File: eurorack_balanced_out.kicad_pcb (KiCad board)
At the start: 2 copper layers, 60 x 35 mm, 31 parts, among them J1 Conn_01x02, J2 Conn_01x02, J3 Conn_02x05_Odd_Even, J4 AudioJack3, J5 AudioJack3, U1 THAT1646W16, U2 THAT1646W16

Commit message: more cleanup
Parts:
- moved D2 1.00 mm to (164.5, 147.0)
- moved D4 1.00 mm to (169.5, 147.0)
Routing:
- net Vcc: track 24.3 -> 0.00 mm, vias 1 -> 0
- net Vee: track 26.3 -> 6.50 mm, vias 1 -> 0
- net Net-(C5-Pad1): track 15.2 -> 24.0 mm
- net Net-(R2-Pad1): track 7.60 -> 4.60 mm
- net Net-(R1-Pad1): track 7.60 -> 4.60 mm
- net Net-(C7-Pad1): track 23.9 -> 25.0 mm
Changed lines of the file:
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@@
     (thickness 1.6)
     (drawings 4)
-    (tracks 95)
+    (tracks 84)
     (zones 0)
     (modules 31)
@@
   (layers
     (0 F.Cu signal)
-    (31 B.Cu signal)
+    (31 B.Cu signal hide)
     (32 B.Adhes user)
     (33 F.Adhes user)
@@
   )
   (module Package_TO_SOT_SMD:SOT-23 (layer F.Cu)
-    (at 163.5 147 90)
+    (at 164.5 147 90)
     (descr "SOT-23, Standard")
     (tags SOT-23)
@@
   )
   (module Package_TO_SOT_SMD:SOT-23 (layer F.Cu)
-    (at 170.5 147 90)
+    (at 169.5 147 90)
     (descr "SOT-23, Standard")
     (tags SOT-23)
@@
   (segment (start 137.35 140.135) (end 138.635 140.135) (width 1) (layer F.Cu) (net 1))
   (segment (start 138.635 140.135) (end 139 140.5) (width 1) (layer F.Cu) (net 1))
-  (segment (start 123 137) (end 125.54 137) (width 1) (layer B.Cu) (net 2))
-  (segment (start 126.2 120.7) (end 124.5 119) (width 1) (layer F.Cu) (net 2))
-  (segment (start 126.2 121) (end 126.2 120.7) (width 1) (layer F.Cu) (net 2))
-  (segment (start 123 124.2) (end 126.2 121) (width 1) (layer F.Cu) (net 2))
-  (segment (start 123 137) (end 123 124.2) (width 1) (layer F.Cu) (net 2))
-  (via (at 145 140) (size 0.8) (drill 0.4) (layers F.Cu B.Cu) (net 2))
-  (segment (start 145.135 140.135) (end 145 140) (width 1) (layer F.Cu) (net 2))
-  (segment (start 146.65 140.135) (end 145.135 140.135) (width 1) (layer F.Cu) (net 2))
-  (segment (start 123 147.16) (end 125.54 147.16) (width 1) (layer B.Cu) (net 3))
-  (via (at 145 142) (size 0.8) (drill 0.4) (layers F.Cu B.Cu) (net 3))
-  (segment (start 146.65 141.405) (end 145.595 141.405) (width 1) (layer F.Cu) (net 3))
-  (segment (start 145.595 141.405) (end 145 142) (width 1) (layer F.Cu) (net 3))
+  (segment (start 123 147.16) (end 125.54 147.16) (width 1) (layer F.Cu) (net 3))
+  (segment (start 127 129.8) (end 126.2 129) (width 1) (layer F.Cu) (net 3))
+  (segment (start 127.090001 129.890001) (end 127 129.8) (width 1) (layer F.Cu) (net 3))
   (segment (start 126.2 128.7) (end 124.5 127) (width 1) (layer F.Cu) (net 3))
   (segment (start 126.2 129) (end 126.2 128.7) (width 1) (layer F.Cu) (net 3))
-  (segment (start 127 129.8) (end 126.2 129) (width 1) (layer F.Cu) (net 3))
-  (segment (start 127.090001 129.890001) (end 127 129.8) (width 1) (layer F.Cu) (net 3))
-  (segment (start 127.090001 145.609999) (end 127.090001 129.890001) (width 1) (layer F.Cu) (net 3))
-  (segment (start 125.54 147.16) (end 127.090001 145.609999) (width 1) (layer F.Cu) (net 3))
-  (segment (start 145.625 137.595) (end 146.65 137.595) (width 0.5) (layer F.Cu) (net 4))
   (segment (start 143 134.97) (end 145.625 137.595) (width 0.5) (layer F.Cu) (net 4))
   (segment (start 143 130.05) (end 143 134.97) (width 0.5) (layer F.Cu) (net 4))
   (segment (start 148.205 137.595) (end 146.65 137.595) (width 0.5) (layer F.Cu) (net 4))
   (segment (start 151 134.8) (end 148.205 137.595) (width 0.5) (layer F.Cu) (net 4))
+  (segment (start 145.625 137.595) (end 146.65 137.595) (width 0.5) (layer F.Cu) (net 4))
+  (segment (start 144.5 138.72) (end 145.625 137.595) (width 0.5) (layer F.Cu) (net 4))
+  (segment (start 144.5 146) (end 144.5 138.72) (width 0.5) (layer F.Cu) (net 4))
   (segment (start 150.665 138.865) (end 151 139.2) (width 0.5) (layer F.Cu) (net 5))
   (segment (start 146.65 138.865) (end 150.665 138.865) (width 0.5) (layer F.Cu) (net 5))
@@
   (segment (start 168 134.97) (end 170.625 137.595) (width 0.5) (layer F.Cu) (net 9))
   (segment (start 168 130.05) (end 168 134.97) (width 0.5) (layer F.Cu) (net 9))
-  (segment (start 170.17499 138.04501) (end 170.625 137.595) (width 0.5) (layer F.Cu) (net 9))
   (segment (start 170.625 137.595) (end 171.65 137.595) (width 0.5) (layer F.Cu) (net 9))
-  (segment (start 170.17499 144.72499) (end 170.17499 138.04501) (width 0.5) (layer F.Cu) (net 9))
-  (segment (start 170.5 145.05) (end 170.17499 144.72499) (width 0.5) (layer F.Cu) (net 9))
-  (segment (start 170.5 146) (end 170.5 145.05) (width 0.5) (layer F.Cu) (net 9))
+  (segment (start 169.5 145.05) (end 169.5 146) (width 0.5) (layer F.Cu) (net 9))
+  (segment (start 170.526466 138.11499) (end 169.5 139.141456) (width 0.5) (layer F.Cu) (net 9))
+  (segment (start 171.43001 138.11499) (end 170.526466 138.11499) (width 0.5) (layer F.Cu) (net 9))
+  (segment (start 169.5 139.141456) (end 169.5 145.05) (width 0.5) (layer F.Cu) (net 9))
+  (segment (start 171.65 137.895) (end 171.43001 138.11499) (width 0.5) (layer F.Cu) (net 9))
+  (segment (start 171.65 137.595) (end 171.65 137.895) (width 0.5) (layer F.Cu) (net 9))
   (segment (start 160.795 137.595) (end 162.35 137.595) (width 0.5) (layer F.Cu) (net 10))
   (segment (start 158 134.8) (end 160.795 137.595) (width 0.5) (layer F.Cu) (net 10))
   (segment (start 166 134.97) (end 163.375 137.595) (width 0.5) (layer F.Cu) (net 10))
   (segment (start 166 130.05) (end 166 134.97) (width 0.5) (layer F.Cu) (net 10))
-  (segment (start 163.375 137.595) (end 162.35 137.595) (width 0.5) (layer F.Cu) (net 10))
-  (segment (start 164.950009 143.599991) (end 164.950009 139.170009) (width 0.5) (layer F.Cu) (net 10))
-  (segment (start 164.950009 139.170009) (end 163.375 137.595) (width 0.5) (layer F.Cu) (net 10))
-  (segment (start 163.5 145.05) (end 164.950009 143.599991) (width 0.5) (layer F.Cu) (net 10))
-  (segment (start 163.5 146) (end 163.5 145.05) (width 0.5) (layer F.Cu) (net 10))
+  (segment (start 164.5 145.05) (end 164.5 146) (width 0.5) (layer F.Cu) (net 10))
+  (segment (start 164.950009 139.170009) (end 164.950009 144.599991) (width 0.5) (layer F.Cu) (net 10))
+  (segment (start 163.375 137.595) (end 164.950009 139.170009) (width 0.5) (layer F.Cu) (net 10))
+  (segment (start 164.950009 144.599991) (end 164.5 145.05) (width 0.5) (layer F.Cu) (net 10))
+  (segment (start 162.35 137.595) (end 163.375 137.595) (width 0.5) (layer F.Cu) (net 10))
   (segment (start 158.335 138.865) (end 158 139.2) (width 0.5) (layer F.Cu) (net 11))
   (segment (start 162.35 138.865) (end 158.335 138.865) (width 0.5) (layer F.Cu) (net 11))
@@
   (segment (start 157.51 144.54) (end 158 144.05) (width 0.5) (layer F.Cu) (net 17))
   (segment (start 155 144.54) (end 157.51 144.54) (width 0.5) (layer F.Cu) (net 17))
-  (segment (start 133.975 142) (end 134 141.975) (width 0.5) (layer F.Cu) (net 18))
-  (segment (start 130 142) (end 133.975 142) (width 0.5) (layer F.Cu) (net 18))
-  (segment (start 134.57 141.405) (end 137.35 141.405) (width 0.5) (layer F.Cu) (net 18))
-  (segment (start 134 141.975) (end 134.57 141.405) (width 0.5) (layer F.Cu) (net 18))
-  (segment (start 159.545 141.405) (end 162.35 141.405) (width 0.5) (layer F.Cu) (net 19))
-  (segment (start 159 141.95) (end 159.545 141.405) (width 0.5) (layer F.Cu) (net 19))
-  (segment (start 158.95 142) (end 159 141.95) (width 0.5) (layer F.Cu) (net 19))
-  (segment (start 155 142) (end 158.95 142) (width 0.5) (layer F.Cu) (net 19))
+  (segment (start 133 142) (end 135 142) (width 0.5) (layer F.Cu) (net 18))
+  (segment (start 135.595 141.405) (end 137.35 141.405) (width 0.5) (layer F.Cu) (net 18))
+  (segment (start 135 142) (end 135.595 141.405) (width 0.5) (layer F.Cu) (net 18))
+  (segment (start 158 142) (end 160 142) (width 0.5) (layer F.Cu) (net 19))
+  (segment (start 160.595 141.405) (end 162.35 141.405) (width 0.5) (layer F.Cu) (net 19))
+  (segment (start 160 142) (end 160.595 141.405) (width 0.5) (layer F.Cu) (net 19))
   (zone (net 1) (net_name GND) (layer F.Cu) (hatch edge 0.508)
     (connect_pads (clearance 0.508))

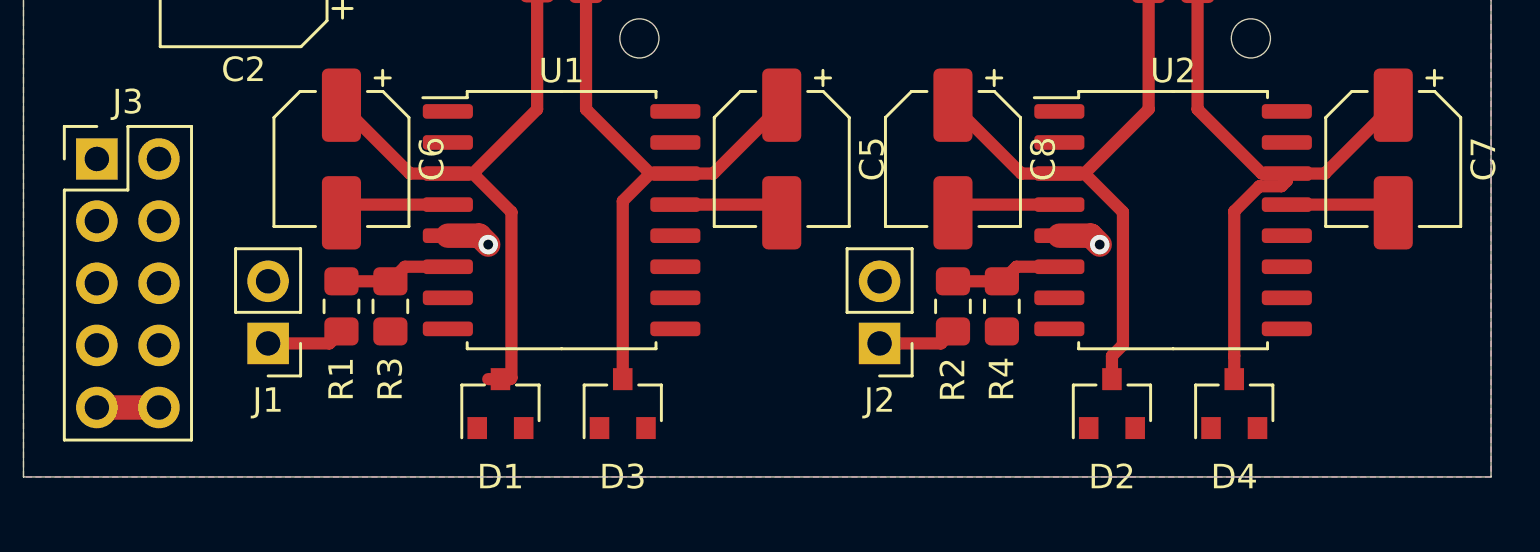
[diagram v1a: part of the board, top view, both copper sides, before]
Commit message: left channel power routing
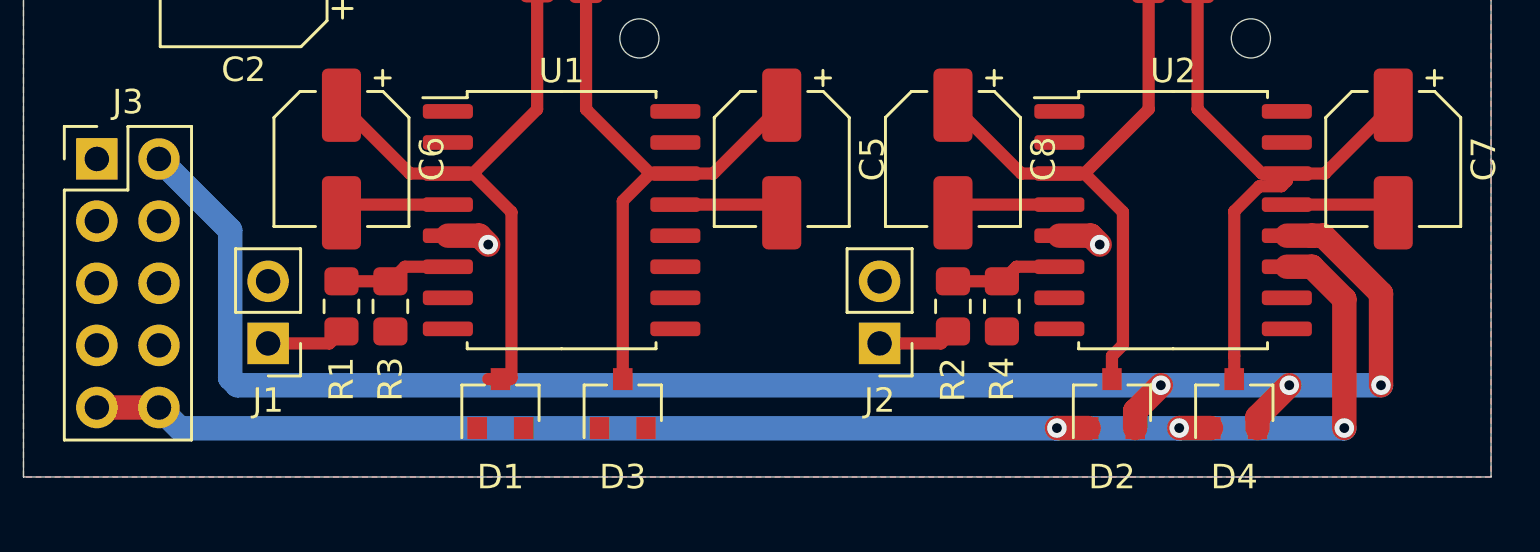
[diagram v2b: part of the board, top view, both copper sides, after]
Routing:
- net Vcc: track 0.00 -> 70.4 mm, vias 0 -> 3
- net Vee: track 6.50 -> 66.1 mm, vias 0 -> 3
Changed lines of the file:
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@@
     (thickness 1.6)
     (drawings 4)
-    (tracks 84)
+    (tracks 116)
     (zones 0)
     (modules 31)
@@
   (layers
     (0 F.Cu signal)
-    (31 B.Cu signal hide)
+    (31 B.Cu signal)
     (32 B.Adhes user)
     (33 F.Adhes user)
@@
   )
   (setup
-    (last_trace_width 0.5)
+    (last_trace_width 1)
     (user_trace_width 0.5)
     (user_trace_width 1)
@@
   (segment (start 137.35 140.135) (end 138.635 140.135) (width 1) (layer F.Cu) (net 1))
   (segment (start 138.635 140.135) (end 139 140.5) (width 1) (layer F.Cu) (net 1))
+  (via (at 175.5 146.25) (size 0.8) (drill 0.4) (layers F.Cu B.Cu) (net 2))
+  (segment (start 128.449999 145.950001) (end 128.749998 146.25) (width 1) (layer B.Cu) (net 2))
+  (segment (start 125.54 137) (end 128.449999 139.909999) (width 1) (layer B.Cu) (net 2))
+  (segment (start 128.449999 139.909999) (end 128.449999 145.950001) (width 1) (layer B.Cu) (net 2))
+  (segment (start 173.135 140.135) (end 172.675 140.135) (width 1) (layer F.Cu) (net 2))
+  (segment (start 172.675 140.135) (end 171.65 140.135) (width 1) (layer F.Cu) (net 2))
+  (segment (start 175.5 142.5) (end 173.135 140.135) (width 1) (layer F.Cu) (net 2))
+  (segment (start 175.5 146.25) (end 175.5 142.5) (width 1) (layer F.Cu) (net 2))
+  (segment (start 171.75 146.25) (end 175.5 146.25) (width 1) (layer B.Cu) (net 2))
+  (via (at 171.75 146.25) (size 0.8) (drill 0.4) (layers F.Cu B.Cu) (net 2))
+  (via (at 166.5 146.25) (size 0.8) (drill 0.4) (layers F.Cu B.Cu) (net 2))
+  (segment (start 166.5 146.25) (end 171.75 146.25) (width 1) (layer B.Cu) (net 2))
+  (segment (start 128.749998 146.25) (end 166.5 146.25) (width 1) (layer B.Cu) (net 2))
+  (segment (start 165.45 147.3) (end 166.5 146.25) (width 1) (layer F.Cu) (net 2))
+  (segment (start 165.45 148) (end 165.45 147.3) (width 1) (layer F.Cu) (net 2))
+  (segment (start 170.45 147.55) (end 171.75 146.25) (width 1) (layer F.Cu) (net 2))
+  (segment (start 170.45 148) (end 170.45 147.55) (width 1) (layer F.Cu) (net 2))
   (segment (start 123 147.16) (end 125.54 147.16) (width 1) (layer F.Cu) (net 3))
   (segment (start 127 129.8) (end 126.2 129) (width 1) (layer F.Cu) (net 3))
@@
   (segment (start 126.2 128.7) (end 124.5 127) (width 1) (layer F.Cu) (net 3))
   (segment (start 126.2 129) (end 126.2 128.7) (width 1) (layer F.Cu) (net 3))
+  (via (at 174 148) (size 0.8) (drill 0.4) (layers F.Cu B.Cu) (net 3))
+  (segment (start 173.990001 148.009999) (end 174 148) (width 1) (layer B.Cu) (net 3))
+  (segment (start 125.54 147.16) (end 126.389999 148.009999) (width 1) (layer B.Cu) (net 3))
+  (segment (start 172.675 141.405) (end 171.65 141.405) (width 1) (layer F.Cu) (net 3))
+  (segment (start 174 142.73) (end 172.675 141.405) (width 1) (layer F.Cu) (net 3))
+  (segment (start 174 148) (end 174 142.73) (width 1) (layer F.Cu) (net 3))
+  (via (at 167.25 148) (size 0.8) (drill 0.4) (layers F.Cu B.Cu) (net 3))
+  (segment (start 167.240001 148.009999) (end 167.25 148) (width 1) (layer B.Cu) (net 3))
+  (segment (start 167.240001 148.009999) (end 173.990001 148.009999) (width 1) (layer B.Cu) (net 3))
+  (via (at 162.25 148) (size 0.8) (drill 0.4) (layers F.Cu B.Cu) (net 3))
+  (segment (start 162.240001 148.009999) (end 167.240001 148.009999) (width 1) (layer B.Cu) (net 3))
+  (segment (start 162.240001 148.009999) (end 162.25 148) (width 1) (layer B.Cu) (net 3))
+  (segment (start 126.389999 148.009999) (end 162.240001 148.009999) (width 1) (layer B.Cu) (net 3))
+  (segment (start 167.25 148) (end 168.55 148) (width 1) (layer F.Cu) (net 3))
+  (segment (start 162.25 148) (end 163.55 148) (width 1) (layer F.Cu) (net 3))
   (segment (start 143 134.97) (end 145.625 137.595) (width 0.5) (layer F.Cu) (net 4))
   (segment (start 143 130.05) (end 143 134.97) (width 0.5) (layer F.Cu) (net 4))

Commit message: rout rest of power
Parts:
- moved C3 24.0 mm to (124.0, 142.0), turned to 0 degrees
- moved J3 21.8 mm to (132.6, 117.5), turned to 270 degrees
- moved C1 16.5 mm to (125.0, 137.0), turned to 180 degrees
- moved C2 4.00 mm to (125.0, 129.0)
- moved C4 2.04 mm to (124.0, 124.0), turned to 0 degrees
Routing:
- net Vee: track 66.1 -> 102.9 mm, vias 3 -> 7
- net Vcc: track 70.4 -> 104.5 mm, vias 3 -> 7

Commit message: small track cleanup
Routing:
- net Vcc: track 104.5 -> 107.1 mm
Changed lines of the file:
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@@
     (thickness 1.6)
     (drawings 4)
-    (tracks 157)
+    (tracks 155)
     (zones 0)
     (modules 31)
@@
   )
   (setup
-    (last_trace_width 1)
+    (last_trace_width 0.5)
     (user_trace_width 0.5)
     (user_trace_width 1)
@@
   (gr_line (start 180 150) (end 120 150) (layer Edge.Cuts) (width 0.05))
   (gr_line (start 180 115) (end 180 150) (layer Edge.Cuts) (width 0.05))
-  (via (at 164 140.5) (size 0.8) (drill 0.4) (layers F.Cu B.Cu) (net 1))
-  (segment (start 162.35 140.135) (end 163.635 140.135) (width 1) (layer F.Cu) (net 1))
-  (segment (start 163.635 140.135) (end 164 140.5) (width 1) (layer F.Cu) (net 1))
-  (via (at 139 140.5) (size 0.8) (drill 0.4) (layers F.Cu B.Cu) (net 1))
-  (segment (start 137.35 140.135) (end 138.635 140.135) (width 1) (layer F.Cu) (net 1))
-  (segment (start 138.635 140.135) (end 139 140.5) (width 1) (layer F.Cu) (net 1))
+  (via (at 135.5 140.2) (size 0.8) (drill 0.4) (layers F.Cu B.Cu) (net 1))
+  (via (at 160.5 140.2) (size 0.8) (drill 0.4) (layers F.Cu B.Cu) (net 1))
+  (segment (start 160.565 140.135) (end 160.5 140.2) (width 1) (layer F.Cu) (net 1))
+  (segment (start 162.35 140.135) (end 160.565 140.135) (width 1) (layer F.Cu) (net 1))
+  (segment (start 135.565 140.135) (end 135.5 140.2) (width 1) (layer F.Cu) (net 1))
+  (segment (start 137.35 140.135) (end 135.565 140.135) (width 1) (layer F.Cu) (net 1))
   (via (at 175.5 146.25) (size 0.8) (drill 0.4) (layers F.Cu B.Cu) (net 2))
   (segment (start 173.135 140.135) (end 172.675 140.135) (width 1) (layer F.Cu) (net 2))
@@
   (segment (start 145.45 147.55) (end 146.75 146.25) (width 1) (layer F.Cu) (net 2))
   (segment (start 145.45 148) (end 145.45 147.55) (width 1) (layer F.Cu) (net 2))
+  (segment (start 132.62 120) (end 132.62 117.46) (width 1) (layer F.Cu) (net 2))
   (via (at 174 148) (size 0.8) (drill 0.4) (layers F.Cu B.Cu) (net 3))
   (segment (start 173.990001 148.009999) (end 174 148) (width 1) (layer B.Cu) (net 3))
@@
   (segment (start 138.375 137.595) (end 141 134.97) (width 0.5) (layer F.Cu) (net 7))
   (segment (start 133 134.8) (end 135.795 137.595) (width 0.5) (layer F.Cu) (net 7))
+  (segment (start 139 146) (end 139.9 146) (width 0.5) (layer F.Cu) (net 7))
   (segment (start 138.375 137.595) (end 137.35 137.595) (width 0.5) (layer F.Cu) (net 7))
-  (segment (start 139.950009 139.170009) (end 138.375 137.595) (width 0.5) (layer F.Cu) (net 7))
-  (segment (start 139.950009 145.949991) (end 139.950009 139.170009) (width 0.5) (layer F.Cu) (net 7))
-  (segment (start 139.9 146) (end 139.950009 145.949991) (width 0.5) (layer F.Cu) (net 7))
-  (segment (start 139 146) (end 139.9 146) (width 0.5) (layer F.Cu) (net 7))
+  (segment (start 139.5 138.72) (end 138.375 137.595) (width 0.5) (layer F.Cu) (net 7))
+  (segment (start 139.5 146) (end 139.5 138.72) (width 0.5) (layer F.Cu) (net 7))
   (segment (start 175.665 138.865) (end 176 139.2) (width 0.5) (layer F.Cu) (net 8))
   (segment (start 171.65 138.865) (end 175.665 138.865) (width 0.5) (layer F.Cu) (net 8))
@@
   (segment (start 166 134.97) (end 163.375 137.595) (width 0.5) (layer F.Cu) (net 10))
   (segment (start 166 130.05) (end 166 134.97) (width 0.5) (layer F.Cu) (net 10))
-  (segment (start 164.5 145.05) (end 164.5 146) (width 0.5) (layer F.Cu) (net 10))
-  (segment (start 164.950009 139.170009) (end 164.950009 144.599991) (width 0.5) (layer F.Cu) (net 10))
-  (segment (start 163.375 137.595) (end 164.950009 139.170009) (width 0.5) (layer F.Cu) (net 10))
-  (segment (start 164.950009 144.599991) (end 164.5 145.05) (width 0.5) (layer F.Cu) (net 10))
-  (segment (start 162.35 137.595) (end 163.375 137.595) (width 0.5) (layer F.Cu) (net 10))
+  (segment (start 164.5 138.72) (end 163.375 137.595) (width 0.5) (layer F.Cu) (net 10))
+  (segment (start 163.375 137.595) (end 162.35 137.595) (width 0.5) (layer F.Cu) (net 10))
+  (segment (start 164.5 146) (end 164.5 138.72) (width 0.5) (layer F.Cu) (net 10))
   (segment (start 158.335 138.865) (end 158 139.2) (width 0.5) (layer F.Cu) (net 11))
   (segment (start 162.35 138.865) (end 158.335 138.865) (width 0.5) (layer F.Cu) (net 11))
